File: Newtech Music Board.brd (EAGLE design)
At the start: 133.3 x 79.7 mm, 51 parts, among them J1 SS-30_BOARD_CONNECTOR, U1 74LS10N, U2 74LS174N, U3 4050N, U4 4069N, U5 LM386N-1

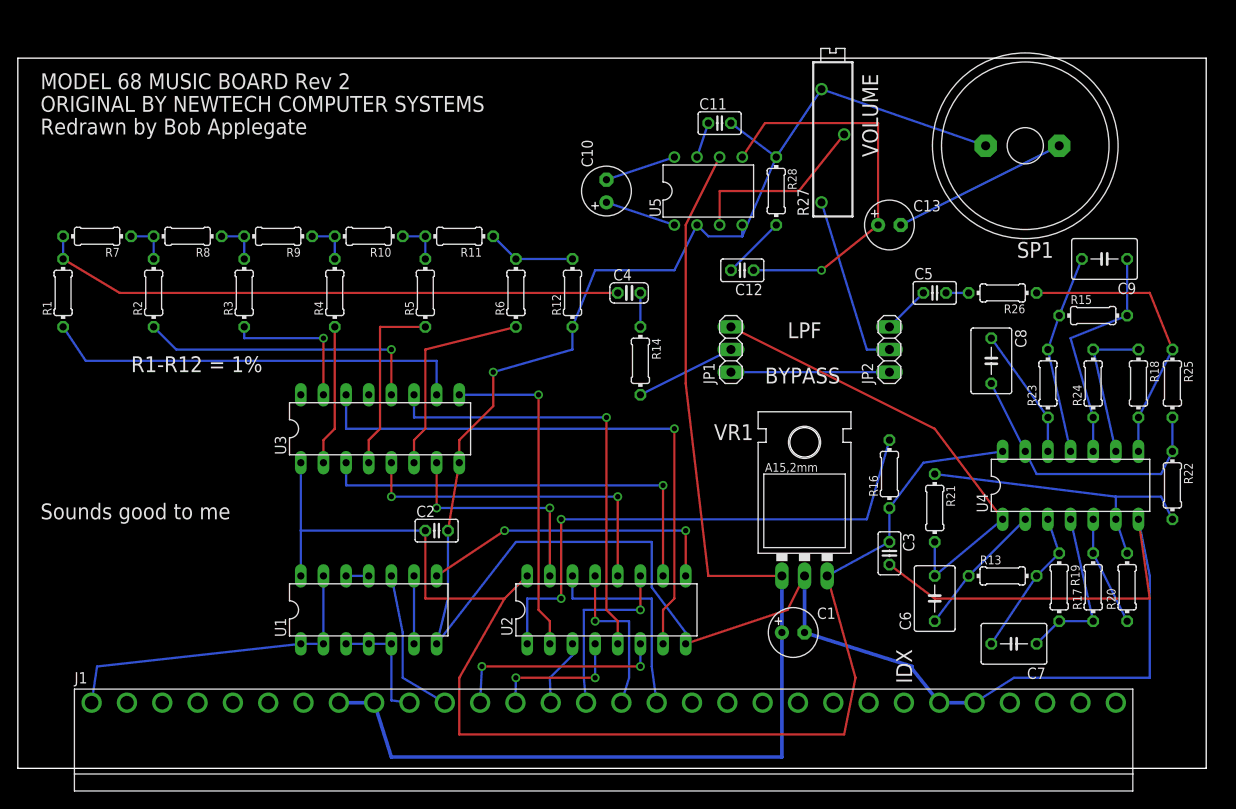
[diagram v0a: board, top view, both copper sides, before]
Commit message: Updated Speaker and incorrect resistor value
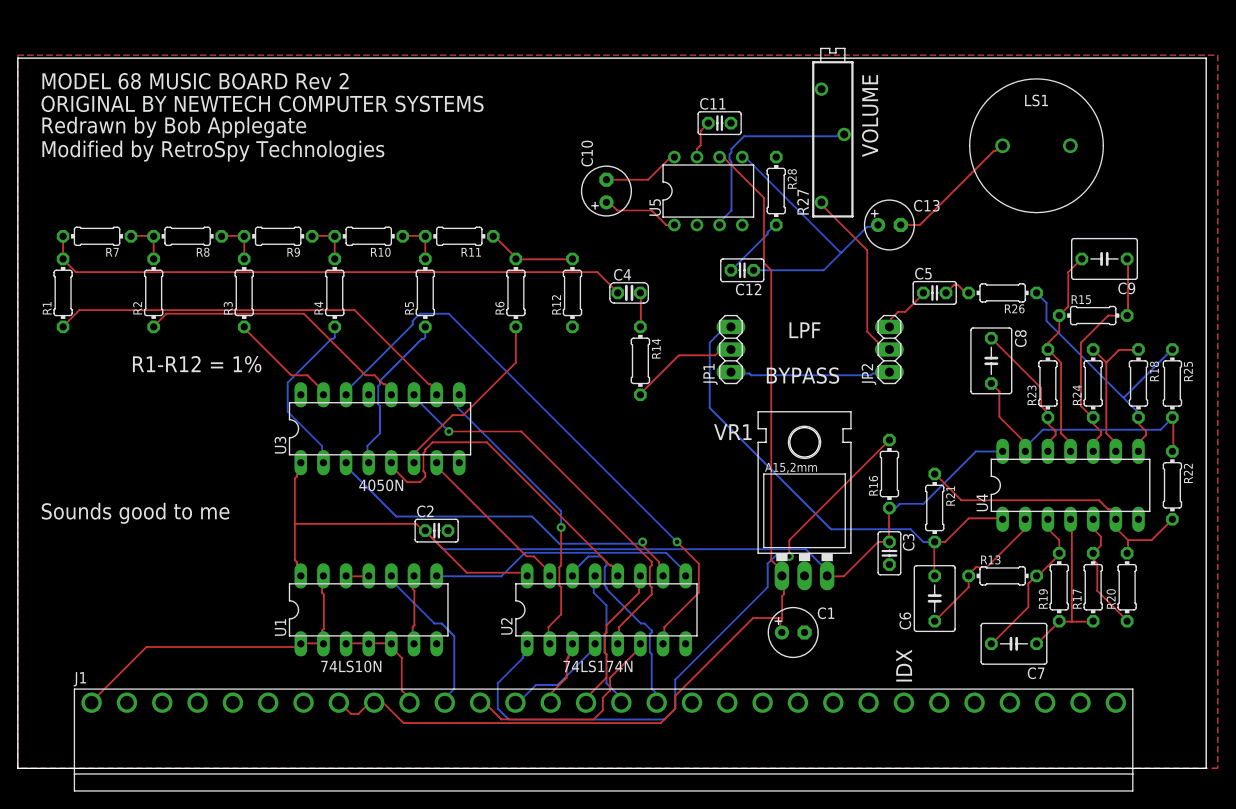
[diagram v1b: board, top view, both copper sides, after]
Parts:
- removed SP1: AL201P, buzzer:AL201P
- added LS1: AST-01508MR-R, AST-01508MR-R:AST01508MRR
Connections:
- net GND: now also LS1.2; no longer SP1.2
- net N$48: now also LS1.1; no longer SP1.1
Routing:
- net GND: track 281.7 -> 0.00 mm, vias 1 -> 0
- net +5V: track 152.0 -> 117.2 mm
- net +8V: track 130.8 -> 114.3 mm
- net N$47: track 44.5 -> 31.7 mm, vias 1 -> 0
- net N$17: track 61.3 -> 70.7 mm, vias 2 -> 1
- net N$14: track 25.4 -> 18.4 mm, vias 2 -> 0
- net N$12: track 48.3 -> 42.1 mm
- net N$48: track 19.9 -> 15.1 mm
- net N$10: track 50.1 -> 45.7 mm
- net N$16: track 34.6 -> 30.4 mm, vias 2 -> 0
- net N$20: track 16.5 -> 12.4 mm, vias 1 -> 0
- net N$9: track 37.4 -> 33.7 mm
- net N$6: track 20.6 -> 17.0 mm, vias 1 -> 0
- net N$2: track 15.5 -> 12.0 mm, vias 2 -> 0
- net N$21: track 15.8 -> 19.3 mm
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- added copper zone on layer 1, net GND
- added copper zone on layer 16, net GND
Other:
- board text added: "Redrawn by Bob Applegate Modified by RetroSpy Technologies"
- board text removed: "Redrawn by Bob Applegate"

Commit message: Added headphone jack out
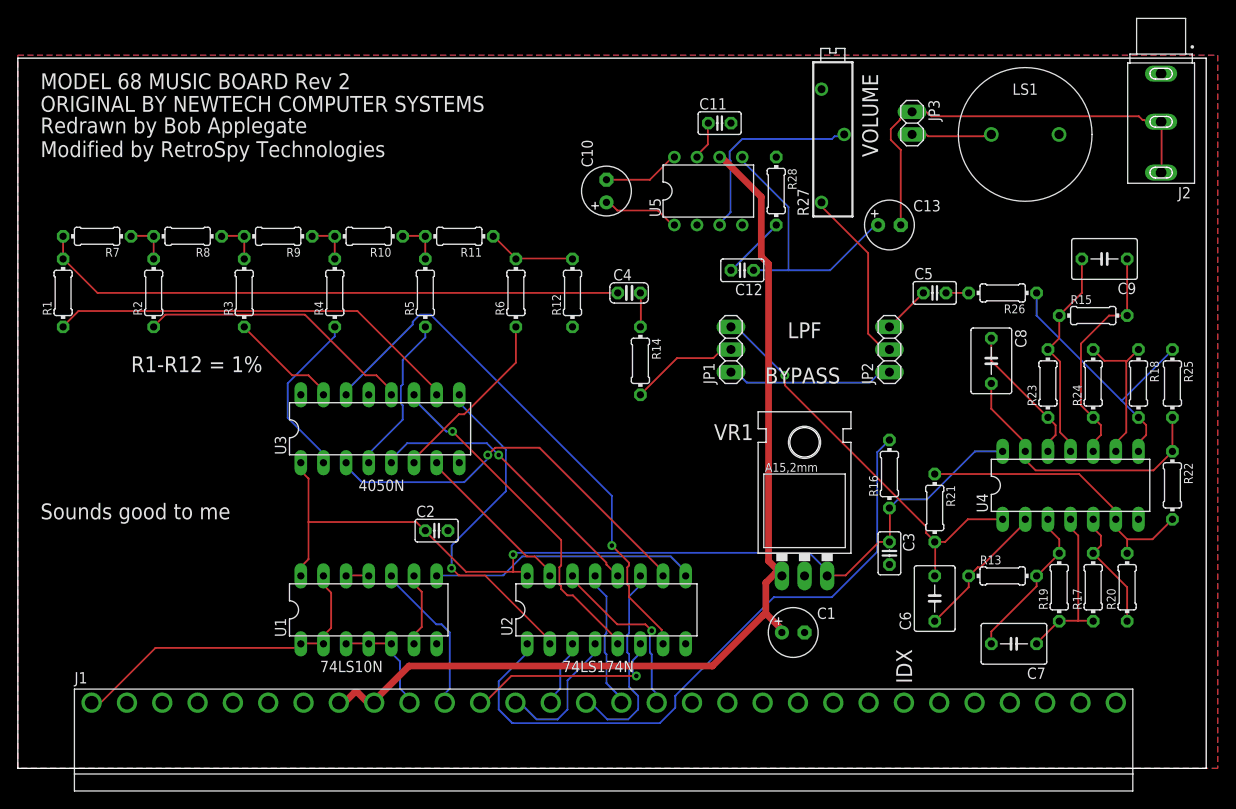
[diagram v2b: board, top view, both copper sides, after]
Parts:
- added J2: MJ-3502N, MJ-3502N:CUI_MJ-3502N
- added JP3: (no value), pinhead:1X02
- moved LS1 1.80 mm to (109.2, 71.1)
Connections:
- new net N$15: JP3.2, LS1.1
- net GND: now also J2.1
- net N$48: now also J2.2, J2.3, JP3.1; no longer LS1.1
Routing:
- net N$48: track 15.1 -> 48.6 mm
- net +5V: track 117.2 -> 107.0 mm, vias 0 -> 1
- net N$15: track 0.00 -> 9.06 mm
- net N$31: track 54.5 -> 46.5 mm, vias 0 -> 1
- net N$10: track 45.7 -> 38.4 mm
- net N$6: track 17.0 -> 23.2 mm
- net N$9: track 33.7 -> 38.9 mm
- net N$11: track 66.1 -> 61.5 mm
- net N$13: track 36.8 -> 32.8 mm, vias 0 -> 1
- net N$2: track 12.0 -> 15.7 mm
- net N$8: track 23.9 -> 20.2 mm, vias 0 -> 1
- net N$17: track 70.7 -> 73.6 mm, vias 1 -> 0
- net N$12: track 42.1 -> 44.8 mm
- net +8V: track 114.3 -> 111.8 mm
- net N$1: track 24.2 -> 22.9 mm, vias 0 -> 1
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
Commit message: Put real speaker on
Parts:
- removed LS1: AST-01508MR-R, AST-01508MR-R:AST01508MRR
- added C14: .0022uF, rcl:C025-025X050
- added JP4: (no value), pinhead:1X02
- added VR2: 3362P-1-253TLF, 3362P-1-253TLF:TRIM_3362P-1-253TLF
- C13: value 10uf, 16v -> 220uF,25v; device rcl:E2,5-6 -> rcl:E25-9
- R13: value 367K -> 357K
- R27: value 5K -> 2M; device resistor:RTRIM43P -> rcl:0204/7
- moved R1 75.5 mm to (76.2, 27.9)
- moved R7 70.7 mm to (76.2, 38.1), turned to 90 degrees
- moved R2 62.5 mm to (72.4, 27.9)
- moved R8 57.5 mm to (72.4, 38.1), turned to 90 degrees
- moved U1 53.6 mm to (67.3, 63.5)
- moved C2 47.6 mm to (80.0, 61.0)
- moved R3 46.9 mm to (64.8, 27.9)
- moved R5 42.7 mm to (80.0, 27.9)
- moved U3 39.5 mm to (73.7, 16.5)
- moved R9 38.4 mm to (61.0, 38.1), turned to 90 degrees
- moved R4 35.9 mm to (61.0, 27.9)
- moved R10 33.3 mm to (64.8, 38.1), turned to 270 degrees
- moved JP3 31.9 mm to (68.6, 74.9), turned to 180 degrees
- moved R11 28.8 mm to (68.6, 38.1), turned to 90 degrees
- moved R6 28.4 mm to (68.6, 27.9)
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- renumbered R14 to R29
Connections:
- removed net N$30: C4.2, R29.1
- new net N$51: C5.1, R29.1
- net DAC_OUT: now also C4.2; no longer R29.2
- net GND: now also C14.2, JP4.2, VR2.1; no longer LS1.2, R27.3
- net LPF_BYPASS: now also R27.2; no longer JP1.1
- net LPF_OUT: now also C14.1, U5.3, VR2.2, VR2.3; no longer R27.1
- net N$15: now also JP4.1; no longer LS1.1
- net N$32: now also R29.2; no longer C5.1
- net N$39: now also JP1.1, R27.1; no longer R27.2, U5.3
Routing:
- net GND: track 0.00 -> 266.3 mm, vias 0 -> 1
- net +5V: track 107.0 -> 173.6 mm, vias 1 -> 0
- net R/!W: track 12.6 -> 66.1 mm
- net PHASE2: track 17.5 -> 69.0 mm
- net !SELECT: track 37.1 -> 83.9 mm
- net N$18: track 46.9 -> 5.42 mm
- net N$29: track 66.4 -> 26.3 mm
- net N$51: track 0.00 -> 40.0 mm
- net N$11: track 61.5 -> 22.9 mm, vias 1 -> 0
- net LPF_OUT: track 20.1 -> 49.8 mm
- net N$12: track 44.8 -> 15.9 mm, vias 1 -> 0
- net N$48: track 48.6 -> 76.8 mm
- net N$14: track 18.5 -> 46.3 mm
- net N$19: track 31.3 -> 4.89 mm
- net N$16: track 30.0 -> 54.8 mm, vias 0 -> 1
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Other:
- board text added: "MODEL 68 MUSIC BOARD RetroSpy Technologies retro-spy.com"
- board text removed: "MODEL 68 MUSIC BOARD Rev 2"
- board text removed: "ORIGINAL BY NEWTECH COMPUTER SYSTEMS"
- board text removed: "R1-R12 = 1%"
- board text removed: "Redrawn by Bob Applegate Modified by RetroSpy Technologies"
- board text removed: "Sounds good to me"

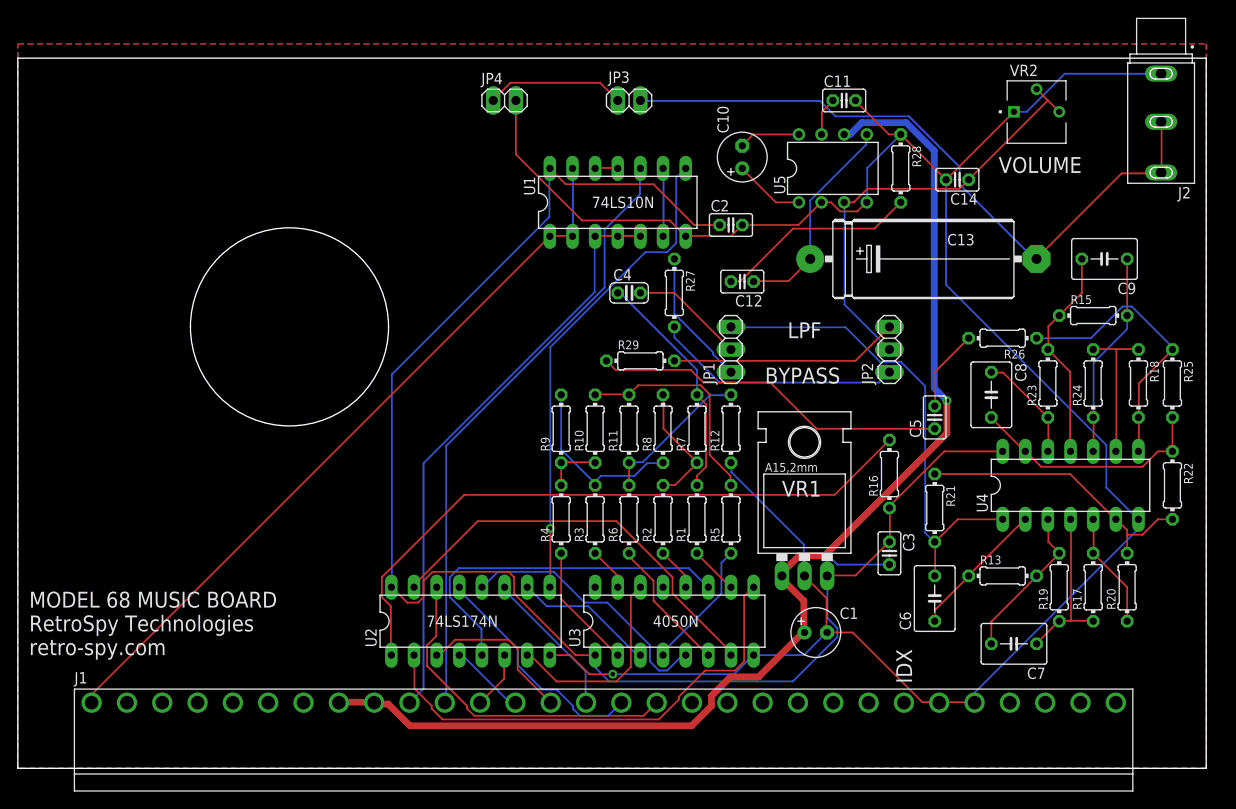
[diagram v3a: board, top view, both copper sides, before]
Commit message: Matched the circuit to the S-100 Board
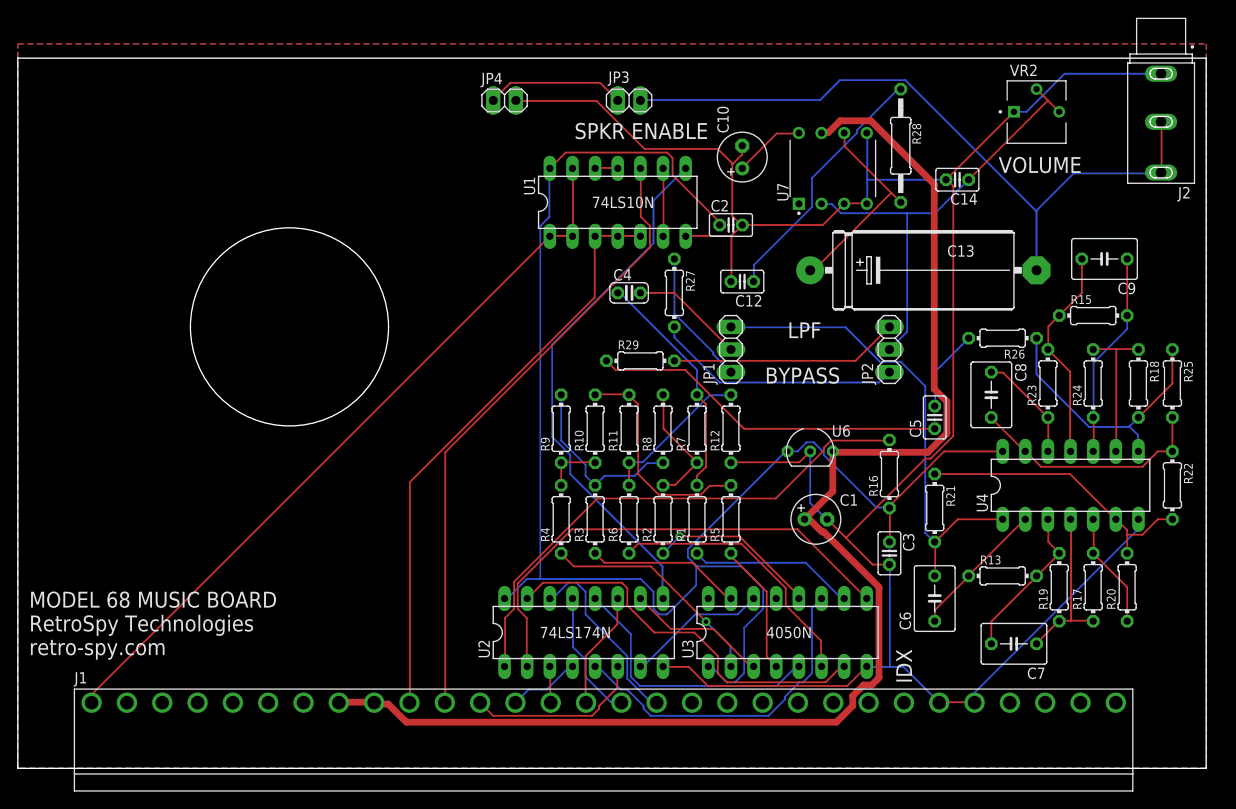
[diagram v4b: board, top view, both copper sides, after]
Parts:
- removed C11: .1uf, rcl:C025-025X050
- removed U5: LM386N-1, linear:DIL08
- removed VR1: 7805, v-reg:78XXL
- added U6: 78L05, 78L05ACZ:TO-92
- added U7: LM380N, LM380N-8_NOPB:DIP794W45P254L959H508Q8
- C1: value 10uf, 16v -> 1uF, 35v
- C10: value 10uf, 16v -> 4.7uF, 10v
- R28: value 10 -> 1; device rcl:0204/7 -> rcl:0207/12
- moved U2 12.8 mm to (63.5, 15.2)
- moved U3 12.8 mm to (86.4, 15.2)
- moved C1 12.7 mm to (89.5, 27.9)
- moved R28 2.54 mm to (99.1, 69.8)
- moved C13 1.27 mm to (101.6, 55.9)
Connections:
- removed net N$44: C11.1, U5.7
- removed net N$46: C10.-, U5.8
- removed net N$50: C12.2, R28.2
- new net N$30: C10.+, U7.8
- net +5V: now also U6.1; no longer VR1.OUT
- net +8V: now also U6.3, U7.7; no longer U5.6, VR1.IN
- net GND: now also C10.-, C12.2, U6.2, U7.3, U7.4, U7.5; no longer C11.2, R28.1, U5.2, U5.4, VR1.GND
- net LPF_OUT: now also U7.2; no longer U5.3
- net N$36: now also C12.1, R28.1; no longer C10.+, U5.1
- net N$47: now also R28.2, U7.6; no longer C12.1, U5.5
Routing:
- net N$50: track 22.7 -> 0.00 mm
- net N$36: track 7.96 -> 28.6 mm
- net +8V: track 135.3 -> 153.2 mm, vias 1 -> 0
- net N$8: track 38.2 -> 21.3 mm
- net N$23: track 15.1 -> 30.6 mm
- net N$19: track 4.89 -> 19.1 mm, vias 0 -> 1
- net N$17: track 72.5 -> 58.8 mm
- net N$3: track 17.8 -> 4.11 mm
- net N$1: track 6.50 -> 19.9 mm
- net N$18: track 5.42 -> 18.6 mm
- net N$20: track 4.89 -> 17.3 mm
- net N$7: track 26.3 -> 14.6 mm
- net N$21: track 14.1 -> 25.6 mm, vias 0 -> 1
- net N$30: track 0.00 -> 8.03 mm
- net N$11: track 22.9 -> 15.9 mm
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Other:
- board text added: "SPKR ENABLE"

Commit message: Put back the LM386
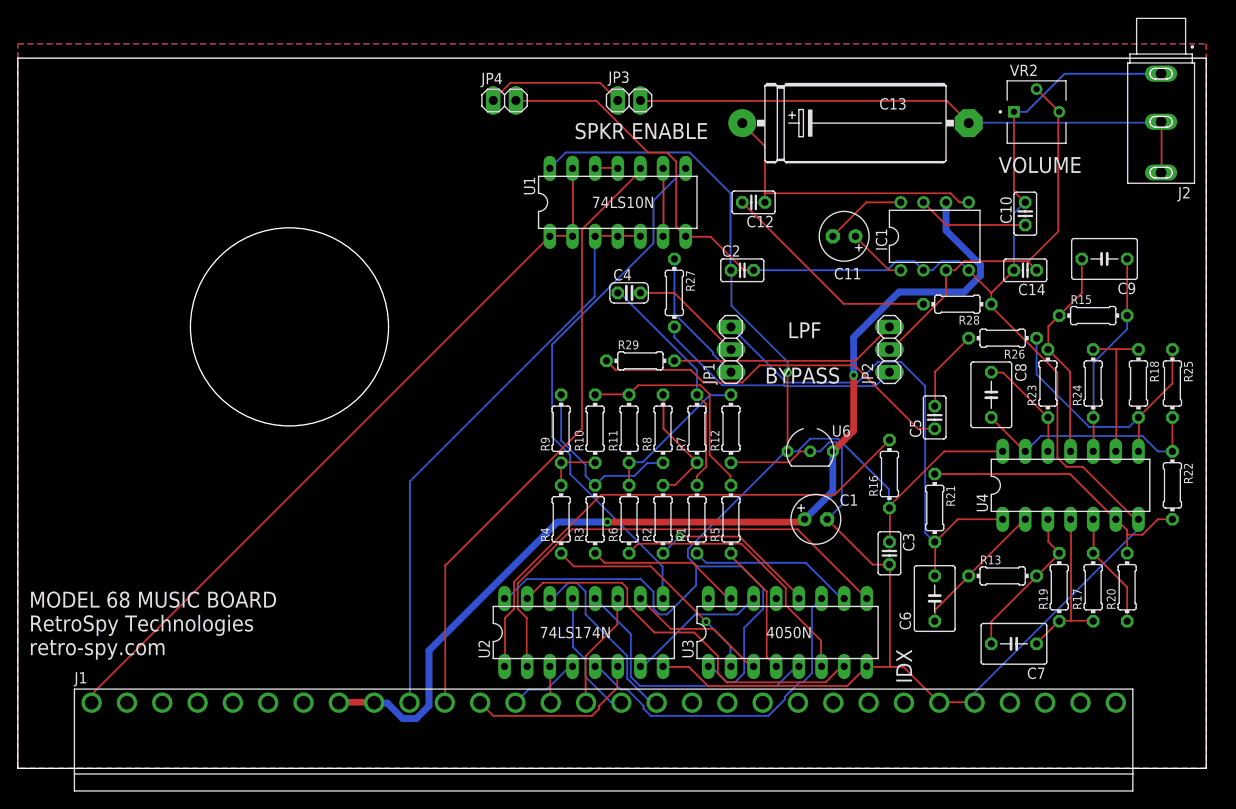
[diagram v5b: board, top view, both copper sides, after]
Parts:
- removed U7: LM380N, LM380N-8_NOPB:DIP794W45P254L959H508Q8
- added C11: 10uF,16V, rcl:E2,5-6
- added IC1: LM386N-1, linear:DIL08
- C10: value 4.7uF, 10v -> .1uF; device rcl:E2,5-6 -> rcl:C025-025X050
- R28: value 1 -> 10; device rcl:0207/12 -> rcl:0204/7
- moved C10 32.4 mm to (113.0, 62.2)
- moved R28 18.9 mm to (105.4, 52.1), turned to 180 degrees
- moved C13 18.2 mm to (94.0, 72.4)
- moved C14 12.7 mm to (113.0, 55.9)
- moved C12 8.98 mm to (82.5, 63.5)
- moved C2 5.24 mm to (81.3, 55.9)
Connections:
- new net N$46: C11.+, IC1.1
- new net N$50: C11.-, IC1.8
- net +8V: now also IC1.6; no longer U7.7
- net GND: now also C10.2, IC1.2, IC1.4, R28.1; no longer C10.-, C12.2, U7.3, U7.4, U7.5
- net LPF_OUT: now also IC1.3; no longer U7.2
- net N$30: now also C10.1, IC1.7; no longer C10.+, U7.8
- net N$36: now also C12.2, R28.2; no longer C12.1, R28.1
- net N$47: now also C12.1, IC1.5; no longer R28.2, U7.6
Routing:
- net +8V: track 153.2 -> 115.5 mm, vias 0 -> 2
- net +5V: track 176.2 -> 161.1 mm, vias 0 -> 1
- net N$48: track 79.7 -> 65.4 mm
- net N$47: track 23.1 -> 33.2 mm
- net N$50: track 0.00 -> 9.23 mm
- net GND: track 261.2 -> 252.3 mm
- net N$46: track 0.00 -> 6.69 mm
- net LPF_OUT: track 50.8 -> 44.6 mm
- net N$30: track 8.03 -> 12.5 mm
- net N$36: track 28.6 -> 25.1 mm
- net N$31: track 55.0 -> 56.9 mm
- net N$51: track 40.0 -> 41.6 mm
- net PHASE2: track 69.9 -> 69.0 mm
- net N$45: track 30.8 -> 31.5 mm

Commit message: Modifcations for prototype
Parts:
- moved J2 12.7 mm to (115.6, 72.4)
- moved VR2 12.7 mm to (127.0, 73.7)
- turned JP4 to 180 degrees
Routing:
- net +8V: track 115.5 -> 138.1 mm, vias 2 -> 0
- net +5V: track 161.1 -> 175.2 mm, vias 1 -> 0
- net N$48: track 65.4 -> 52.6 mm
- net LPF_OUT: track 44.6 -> 50.4 mm
- net N$47: track 33.2 -> 38.0 mm
- net N$45: track 31.5 -> 27.1 mm
- net N$15: track 15.6 -> 11.4 mm
- net GND: track 252.3 -> 249.6 mm
- net N$31: track 56.9 -> 55.0 mm
- net N$42: track 23.2 -> 25.0 mm
- net N$51: track 41.6 -> 40.0 mm

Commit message: Redid the DAC routing
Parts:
- added C15: .1uf, rcl:C025-025X050
- C1: value 1uF, 35v -> .1uf; device rcl:E2,5-6 -> rcl:C025-025X050
- moved R29 33.0 mm to (102.9, 45.7), turned to 90 degrees
- moved U2 24.1 mm to (87.6, 15.2)
- moved R27 21.6 mm to (90.2, 39.4), turned to 0 degrees
- moved U3 21.6 mm to (64.8, 15.2)
- moved R1 15.2 mm to (61.0, 27.9)
- moved R7 15.2 mm to (61.0, 38.1), turned to 270 degrees
- moved R6 11.4 mm to (80.0, 27.9)
- moved R4 11.4 mm to (72.4, 27.9)
- moved R10 7.62 mm to (72.4, 38.1)
- moved R11 7.62 mm to (76.2, 38.1), turned to 270 degrees
- moved R2 7.62 mm to (64.8, 27.9)
- moved R8 7.62 mm to (64.8, 38.1), turned to 270 degrees
- moved R9 7.62 mm to (68.6, 38.1), turned to 270 degrees
- moved C4 6.84 mm to (71.1, 47.0)
- moved C1 5.12 mm to (85.1, 25.4)
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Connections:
- net +5V: now also C1.1
- net +8V: now also C15.1; no longer C1.+
- net GND: now also C1.2, C15.2; no longer C1.-
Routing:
- net +5V: track 175.2 -> 130.9 mm
- net N$9: track 54.6 -> 11.9 mm
- net N$12: track 15.9 -> 48.8 mm, vias 0 -> 1
- net N$51: track 40.0 -> 7.19 mm
- net N$14: track 43.9 -> 13.3 mm
- net N$11: track 15.9 -> 45.4 mm
- net N$2: track 8.08 -> 36.0 mm
- net +8V: track 138.1 -> 112.3 mm
- net N$6: track 13.2 -> 38.3 mm
- net N$3: track 4.11 -> 29.1 mm
- net N$1: track 19.9 -> 44.3 mm
- net LPF_BYPASS: track 27.9 -> 6.66 mm
- net N$32: track 25.7 -> 5.08 mm
- net N$17: track 58.6 -> 41.0 mm, vias 0 -> 2
- net N$19: track 19.1 -> 5.61 mm, vias 1 -> 0
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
